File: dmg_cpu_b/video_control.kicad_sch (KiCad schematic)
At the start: 27 parts

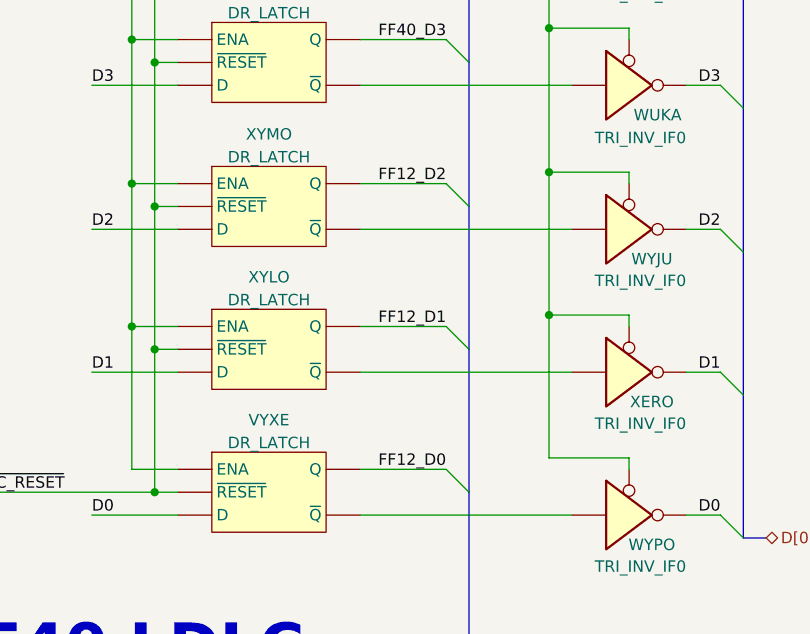
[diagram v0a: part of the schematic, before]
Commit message: Fixes and and rearranged schematics whereever possible to improve legibility.
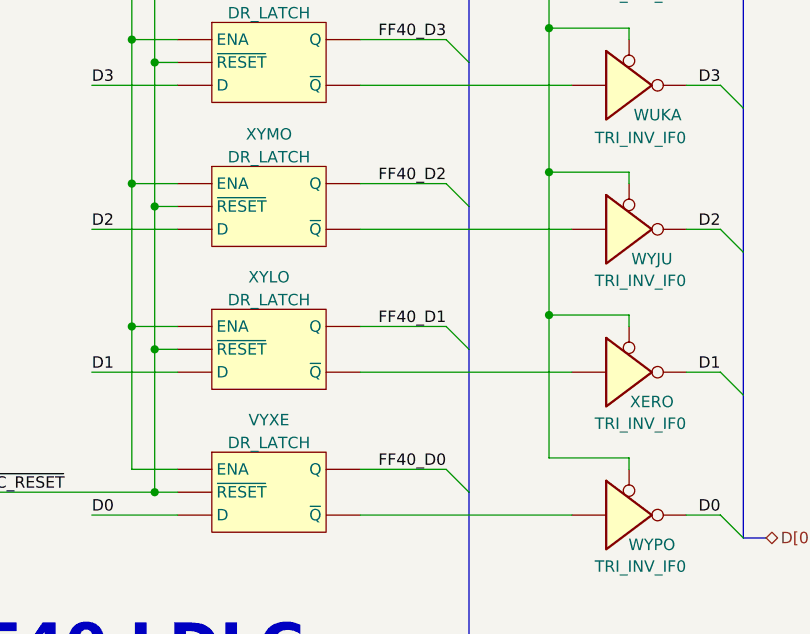
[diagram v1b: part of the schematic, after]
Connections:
- net FF12_D0 renamed FF40_D0
- net FF12_D1 renamed FF40_D1
- net FF12_D2 renamed FF40_D2
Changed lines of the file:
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@@
     (effects (font (size 5 5) (thickness 1) bold) (justify left bottom))
   )
-  (label "FF12_D0" (at 90.17 155.575 180)
+  (label "FF40_D0" (at 90.17 155.575 180)
     (effects (font (size 1.27 1.27)) (justify right bottom))
   )
@@
     (effects (font (size 1.27 1.27)) (justify left bottom))
   )
-  (label "FF12_D1" (at 90.17 139.7 180)
+  (label "FF40_D1" (at 90.17 139.7 180)
     (effects (font (size 1.27 1.27)) (justify right bottom))
   )
@@
     (effects (font (size 1.27 1.27)) (justify right bottom))
   )
-  (label "FF12_D2" (at 90.17 123.825 180)
+  (label "FF40_D2" (at 90.17 123.825 180)
     (effects (font (size 1.27 1.27)) (justify right bottom))
   )

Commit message: VRAM interface sheet added but various edits in existing sheets. Notable merge of RESET, CLOCKS and FF04 DIV sheets
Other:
- company: (none) -> CC-BY-SA-4.0 Régis Galland & Michael Singer -- Derived work from Furrtek
- title: (none) -> DMG CPU B
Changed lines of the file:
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@@
 (kicad_sch (version 20211123) (generator eeschema)
   (paper "A3")
+  (title_block
+    (title "DMG CPU B")
+    (date "2022-05-02")
+    (rev "0")
+    (company "CC-BY-SA-4.0 Régis Galland & Michael Singer -- Derived work from Furrtek")
+    (comment 1 "https://github.com/msinger/dmg-schematics")
+  )
   (junction (at 229.235 65.913) (diameter 0) (color 0 0 0 0)
   )

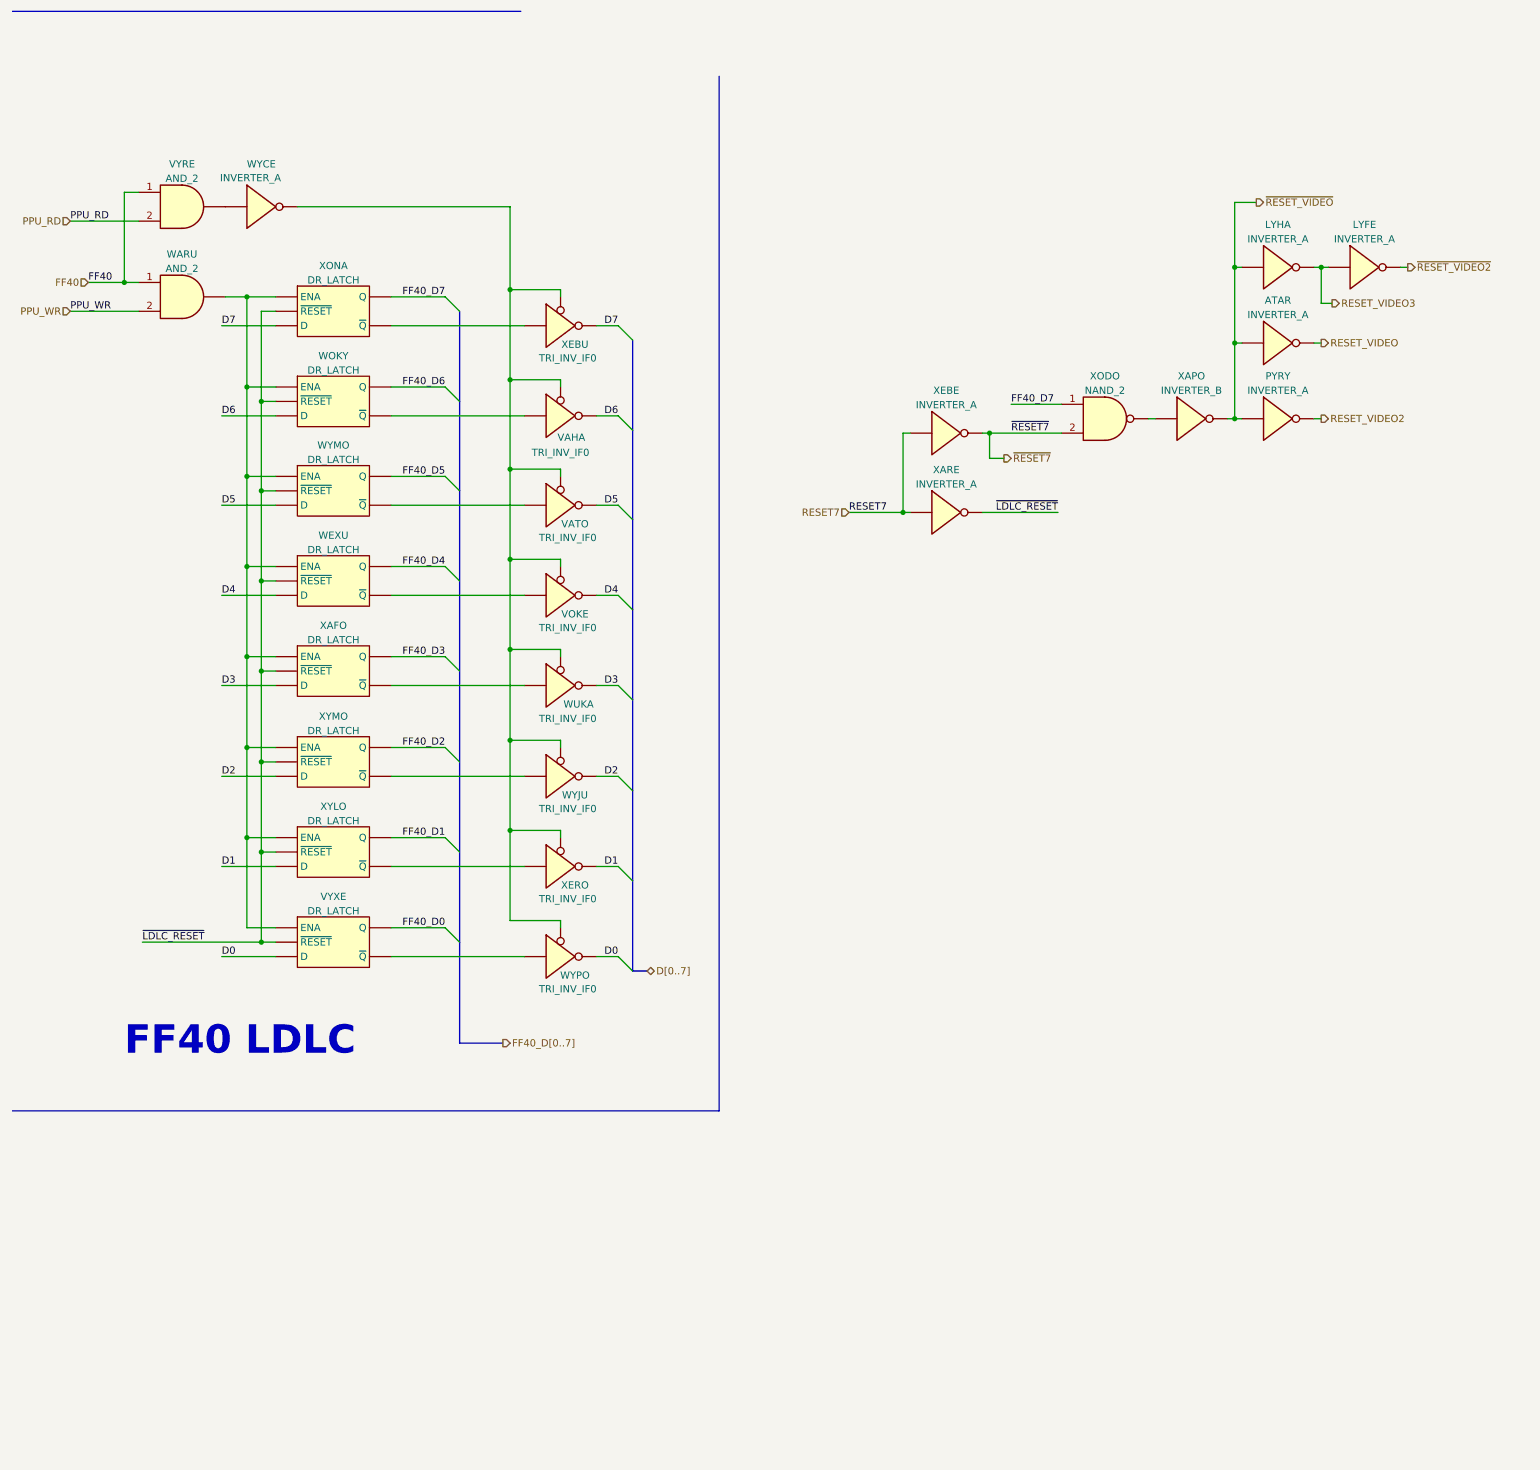
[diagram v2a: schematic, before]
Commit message: OAM and sprite x priority sheets added. OAM sheet still needs some work on it.
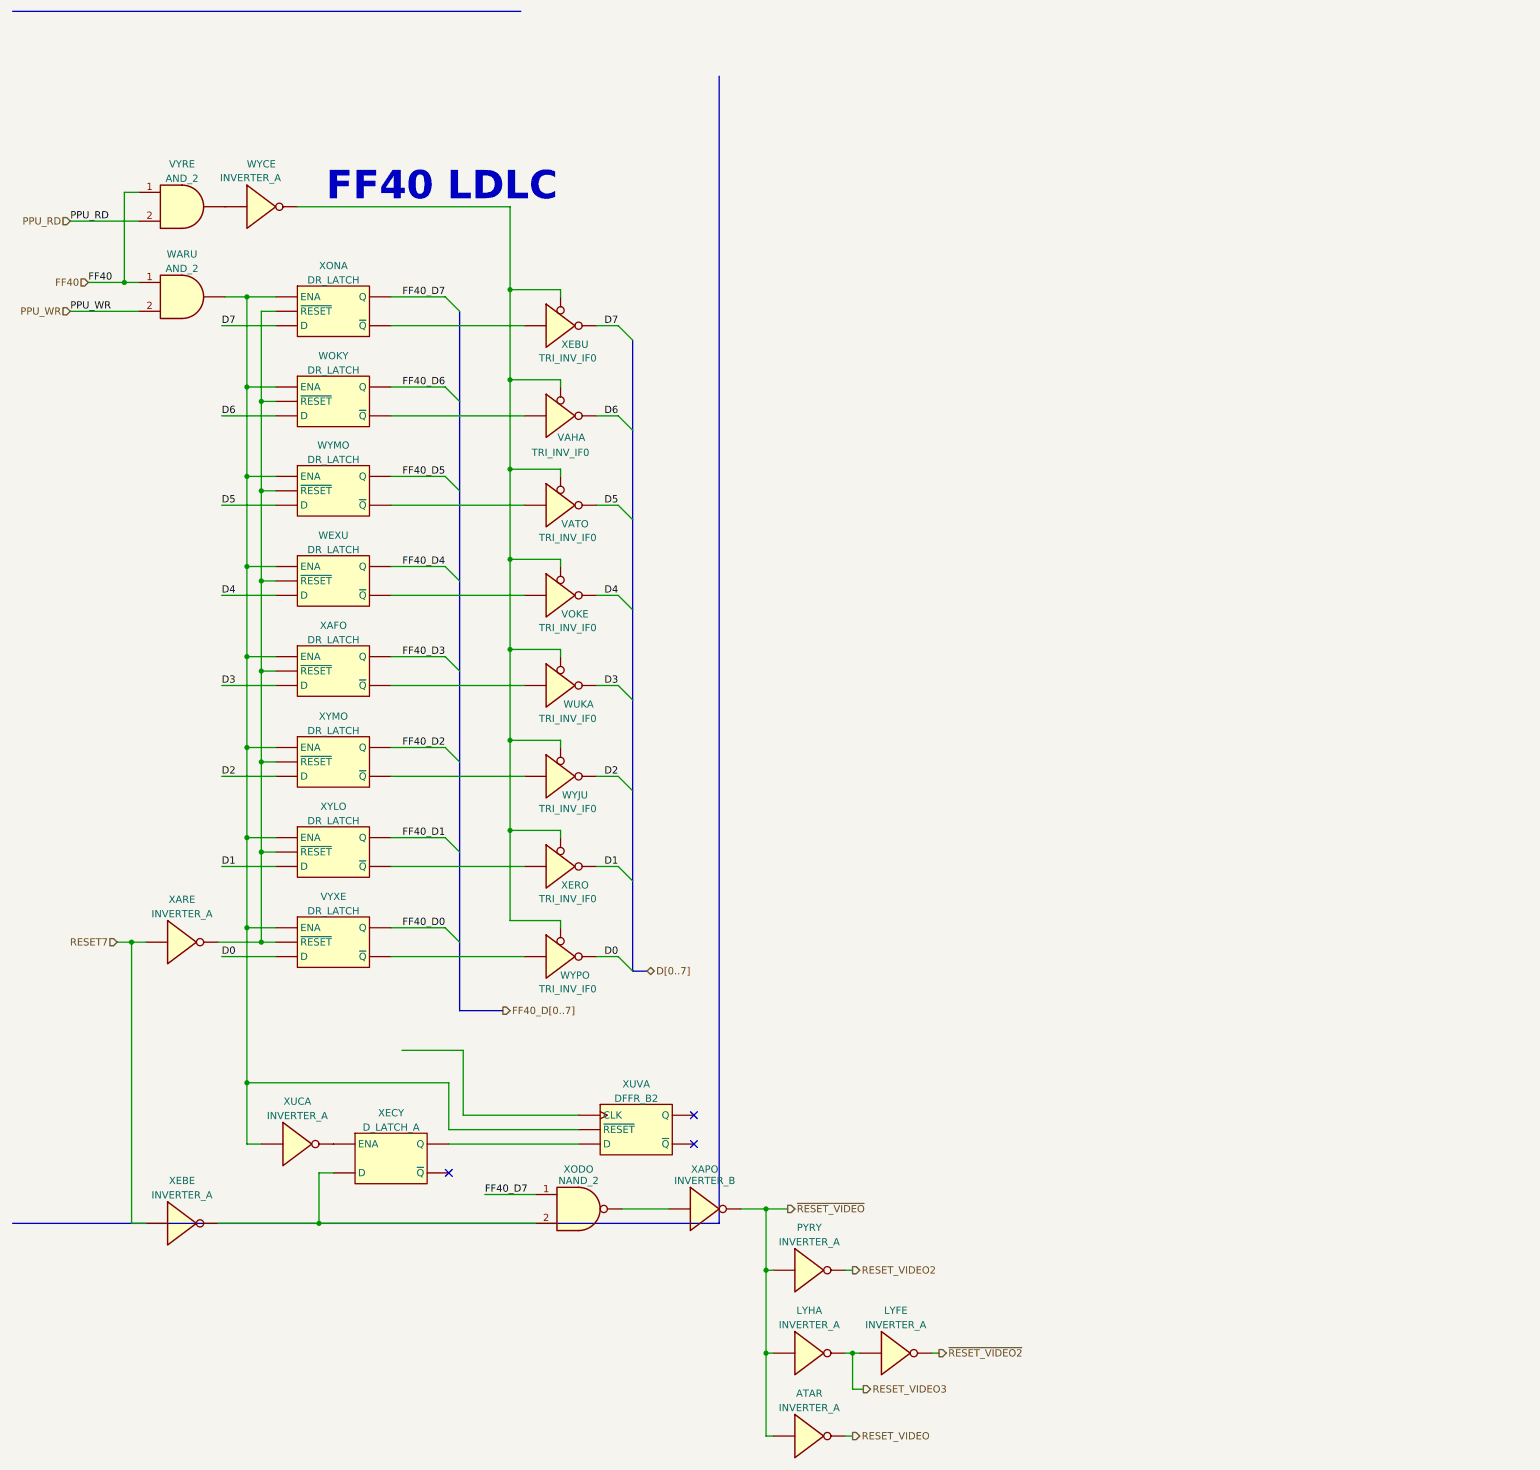
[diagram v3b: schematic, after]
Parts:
- added XECY: D_LATCH_A, symbol DMG_CPU_Cells:D_LATCH_A
- added XUCA: INVERTER_A, symbol DMG_CPU_Cells:INVERTER_A
- added XUVA: DFFR_B2, symbol DMG_CPU_Cells:DFFR_B2
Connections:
- net at VYXE.1 (~{ENA}), VYXE.3 (ENA), WARU.3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: now also XUCA.1, XUVA.2 (~{RESET}), XUVA.4 (~{RESET})
- net ~{LDLC_RESET}: no longer names the net of VYXE.4 (~{RESET}), WEXU.4 (~{RESET}), WOKY.4 (~{RESET}), WYMO.4 (~{RESET}), XAFO.4 (~{RESET}), XARE.2, XONA.4 (~{RESET}), XYLO.4 (~{RESET}), XYMO.4 (~{RESET})
- net ~{RESET7}: no longer names the net of XEBE.2, XODO.2
- net ~{RESET7}: now also XECY.2 (D)
- new net: XECY.1 (~{ENA}), XECY.3 (ENA), XUCA.2
- new net: XECY.4 (Q), XUVA.3 (D)
- no-connect marks 0 -> 3
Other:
- moved on the sheet: ATAR, LYFE, LYHA, PYRY, XAPO, XARE, XEBE, XODO

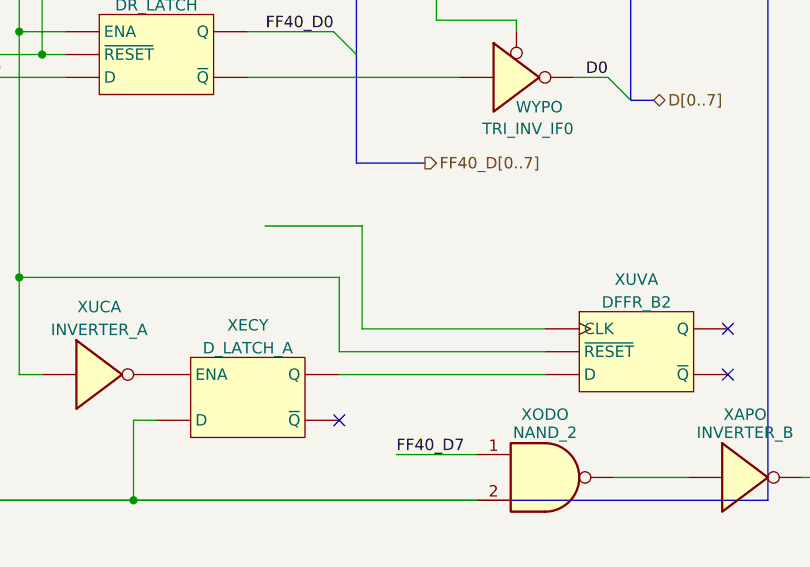
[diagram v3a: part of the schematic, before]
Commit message: More OAM sheets added.
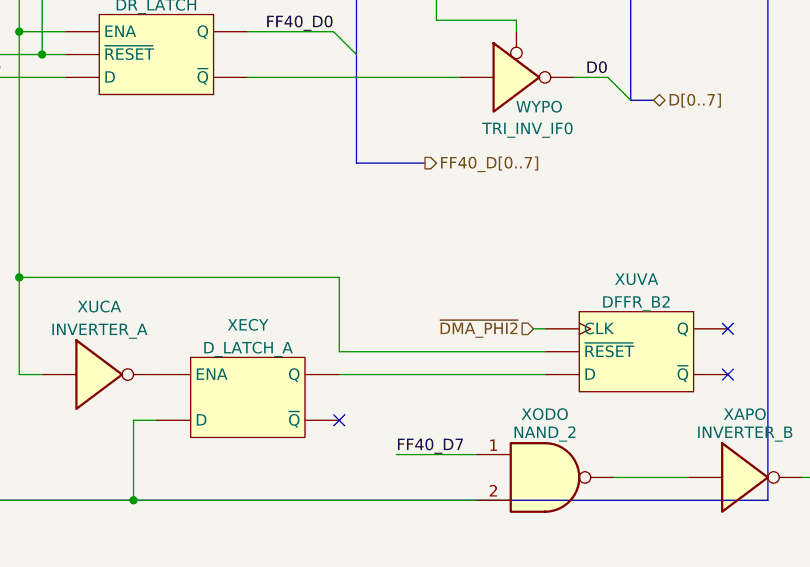
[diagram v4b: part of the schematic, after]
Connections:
- net ~{DMA_PHI2}: now reaches XUVA.1 (CLK)
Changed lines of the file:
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@@
-    (stroke (width 0) (type default) (color 0 0 0 0))
-  )
-  (wire (pts (xy 93.345 177.165) (xy 93.345 188.595))
     (stroke (width 0) (type default) (color 0 0 0 0))
   )
@@
     (stroke (width 0) (type default) (color 0 0 0 0))
   )
-  (wire (pts (xy 82.55 177.165) (xy 93.345 177.165))
+  (wire (pts (xy 112.395 188.595) (xy 113.665 188.595))
     (stroke (width 0) (type default) (color 0 0 0 0))
   )
@@
   )
   (wire (pts (xy 33.655 41.91) (xy 36.195 41.91))
-    (stroke (width 0) (type default) (color 0 0 0 0))
-  )
-  (wire (pts (xy 93.345 188.595) (xy 113.665 188.595))
     (stroke (width 0) (type default) (color 0 0 0 0))
   )
@@
     (effects (font (size 1.27 1.27)) (justify left))
   )
+  (hierarchical_label "~{DMA_PHI2}" (shape input) (at 112.395 188.595 180)
+    (effects (font (size 1.27 1.27)) (justify right))
+  )
   (hierarchical_label "RESET_VIDEO2" (shape output) (at 161.925 215.9 0)
